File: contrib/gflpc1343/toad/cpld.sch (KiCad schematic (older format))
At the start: 30 parts, among them P1 GOODFET, P2 CPLD_JTAG, P4 EXPANSION, U27 DG409, U28 5M80ZT100, U29 GSG-AD5290, U30 DG409, U31 MC4558

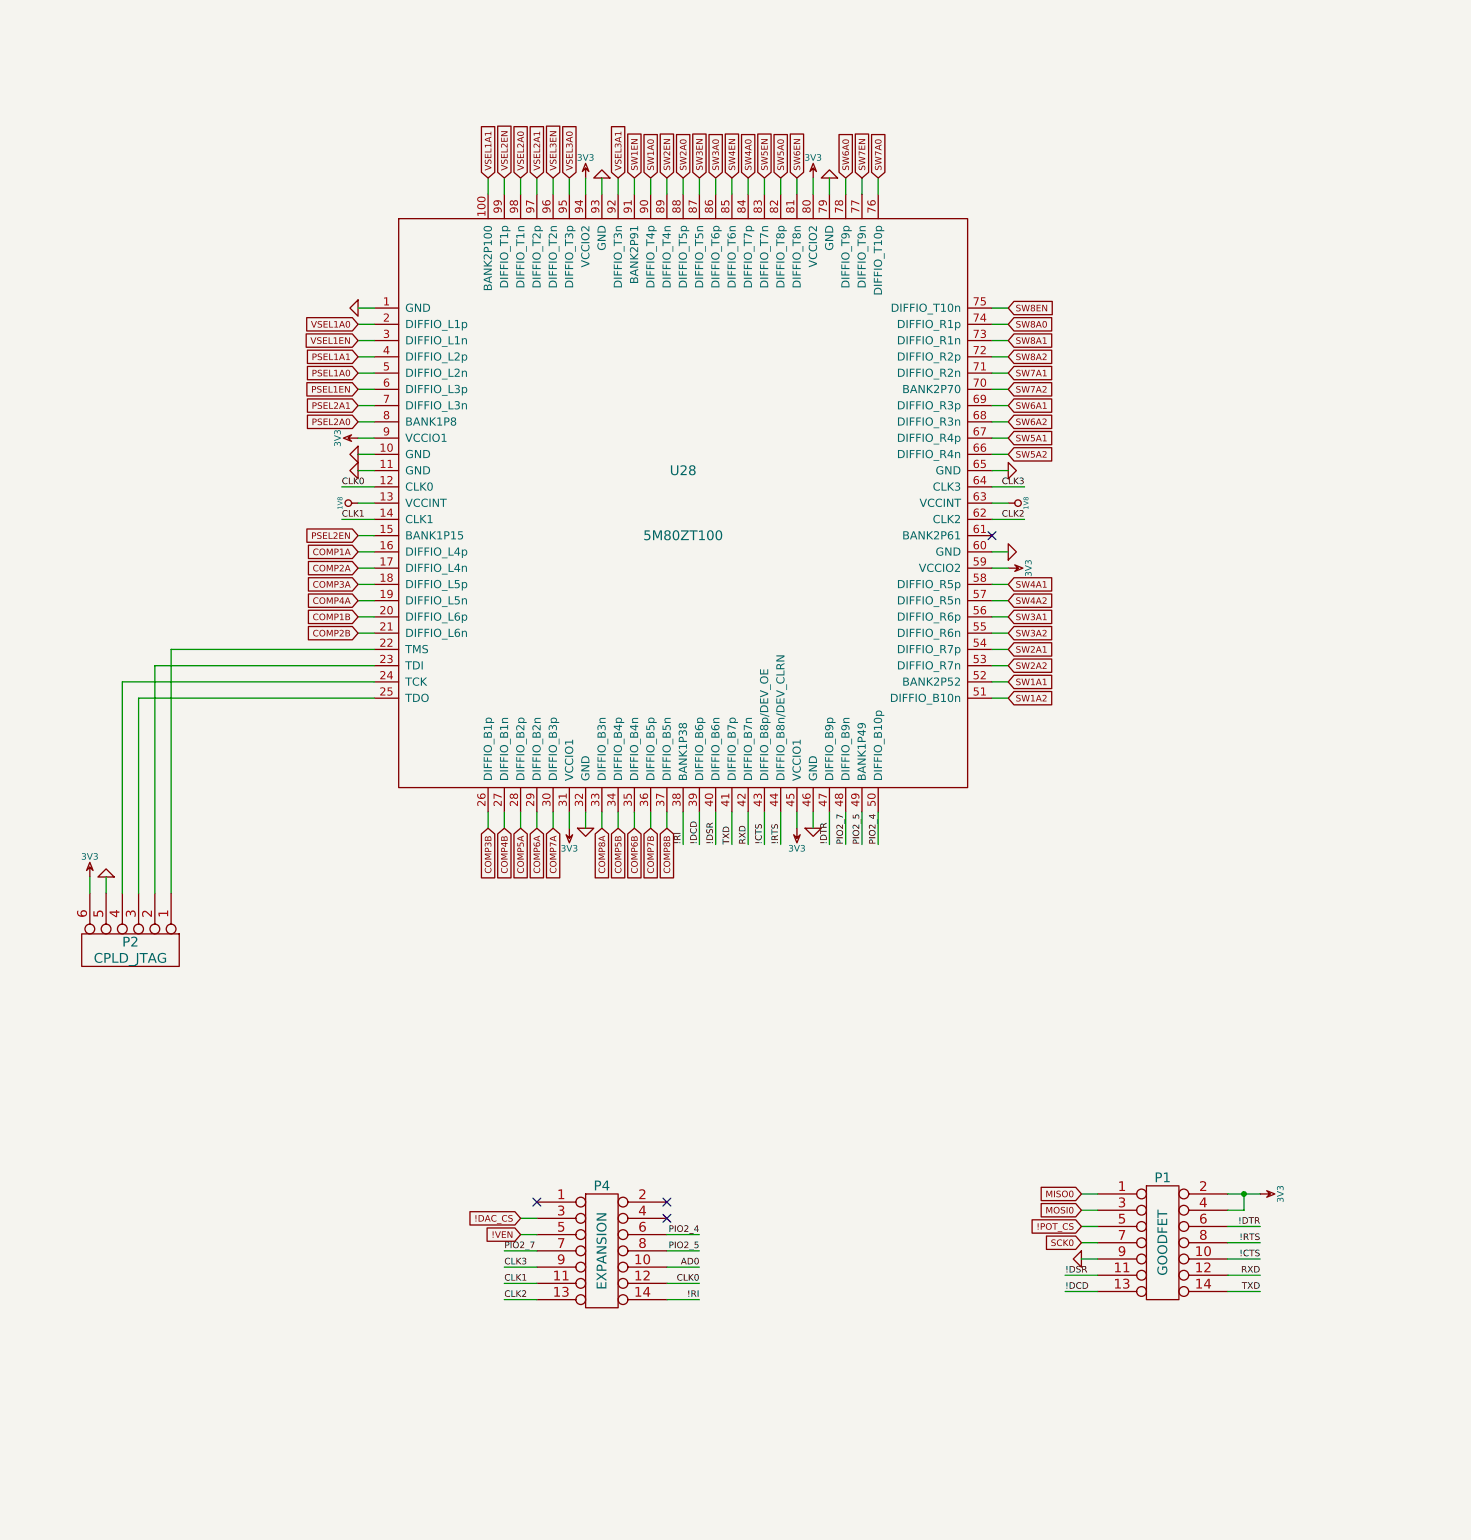
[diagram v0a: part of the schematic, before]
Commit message: TOAD: CPLD decoupling caps, rearranged headers to expose JTAG, etc.
git-svn-id: https://svn.code.sf.net/p/goodfet/code@1622 12e2690d-a6be-4b82-a7b7-67c4a43b65c8
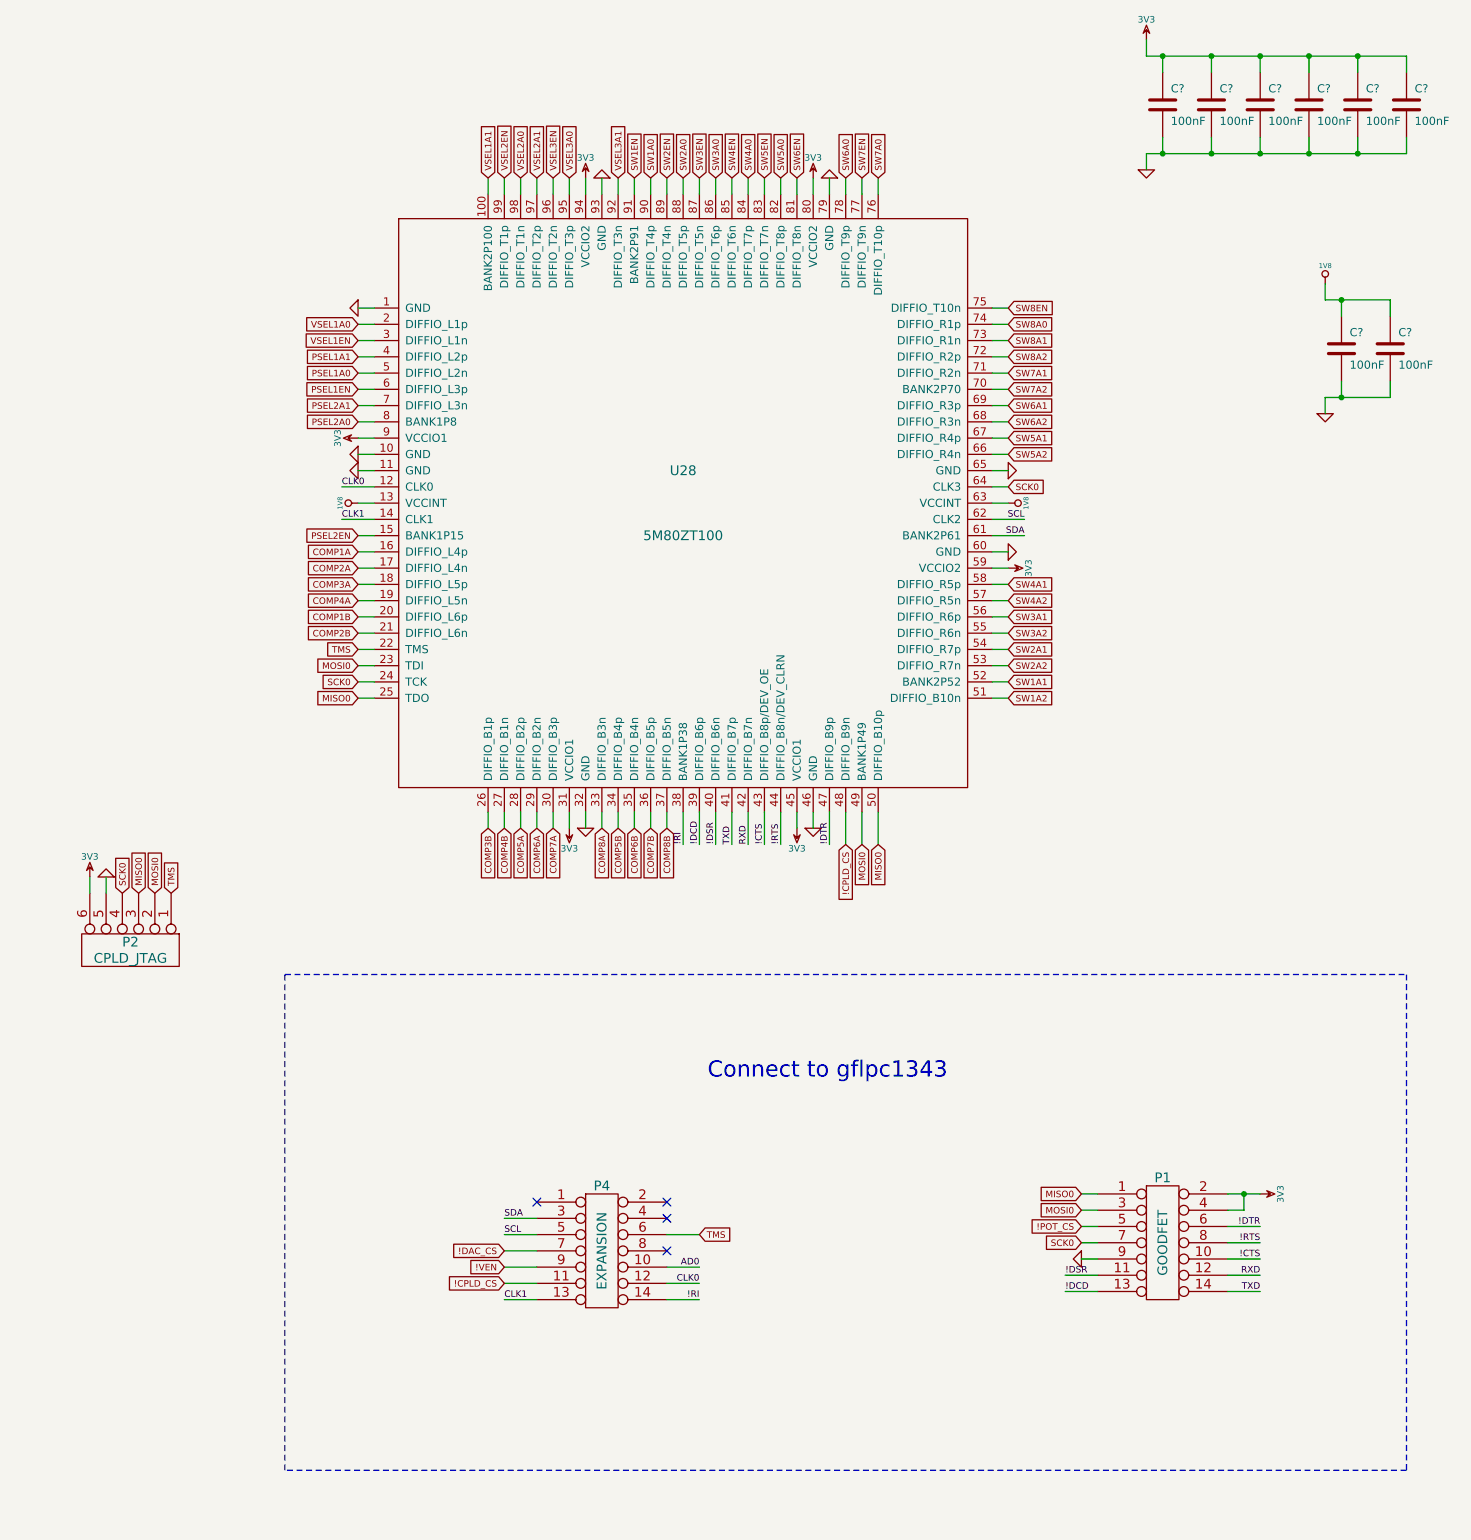
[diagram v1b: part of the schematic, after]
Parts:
- added C? (x8): 100nF, symbol C
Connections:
- net !DAC_CS: now also P4.7 (P7); no longer P4.3 (P3)
- net !VEN: now also P4.9; no longer P4.5 (P5)
- net +1.8V: now also C?.1, C?.1
- net 3V3: now also C?.1, C?.1, C?.1, C?.1, C?.1, C?.1
- net CLK1: now also P4.13; no longer P4.11
- net GND: now also C?.2, C?.2, C?.2, C?.2, C?.2, C?.2, C?.2, C?.2
- net MISO0: now also P2.3, U28.25 (TDO), U28.50 (DIFFIO_B10p)
- net MOSI0: now also P2.2, U28.23 (TDI), U28.49 (BANK1P49)
- net SCK0: now also P2.4, U28.24 (TCK), U28.64 (CLK3)
- net TMS: now reaches P2.1, U28.22 (TMS)
- net TMS: now also P4.6 (P6)
- net SDA: now reaches U28.61 (BANK2P61)
- net SDA: now also P4.3 (P3)
- net CLK2 renamed SCL
- net SCL: now also P4.5 (P5); no longer P4.13
- removed net CLK3: P4.9, U28.64 (CLK3)
- removed net PIO2_4: P4.6 (P6), U28.50 (DIFFIO_B10p)
- net PIO2_5: no longer names the net of P4.8 (P8)
- net PIO2_5: no longer U28.49 (BANK1P49)
- net PIO2_7 renamed !CPLD_CS
- net !CPLD_CS: now also P4.11; no longer P4.7 (P7)
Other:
- note added: "Connect to gflpc1343"

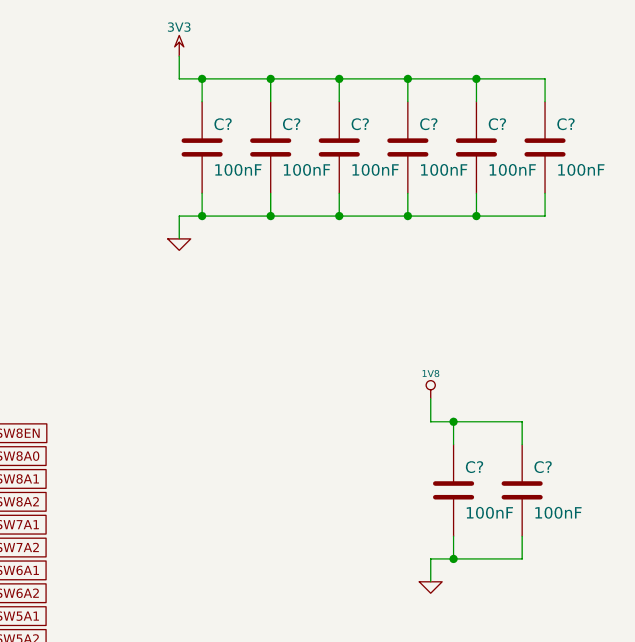
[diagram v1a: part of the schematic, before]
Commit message: TOAD: power indicator LED, some component selection
git-svn-id: https://svn.code.sf.net/p/goodfet/code@1623 12e2690d-a6be-4b82-a7b7-67c4a43b65c8
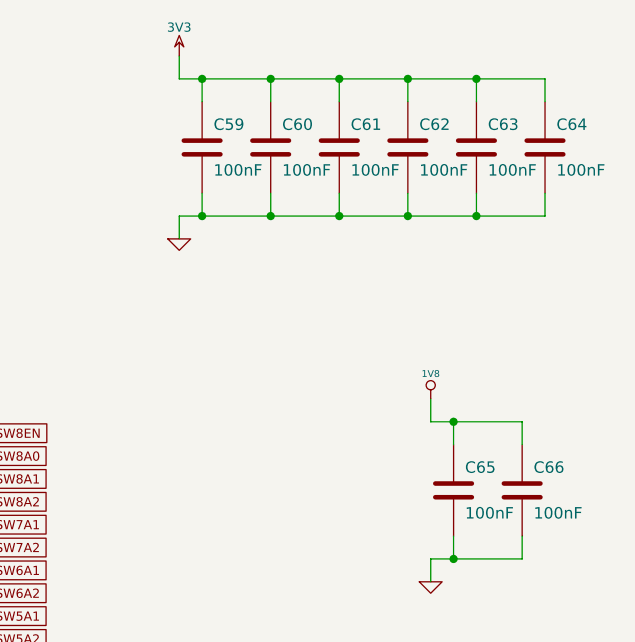
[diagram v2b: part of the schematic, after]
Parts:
- U27, U30: Description (none) -> IC MUX CMOS ANG DUAL 8CH 16TSSOP; Manufacturer (none) -> Vishay Siliconix; Part Number (none) -> DG409LDQ-T1-E3
- U28: Description (none) -> IC MAX V CPLD 80 LE 100-TQFP; Manufacturer (none) -> Altera; Part Number (none) -> 5M80ZT100C5N
- gave numbers to parts that had none: 8

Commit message: TOAD: comparator voltage dividers
git-svn-id: https://svn.code.sf.net/p/goodfet/code@1624 12e2690d-a6be-4b82-a7b7-67c4a43b65c8
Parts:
- added R100, R101, R102, R107, R108, R109, R110, R115, R116, R117, R118, R91, R92, R93, R99: 49.9k, symbol R
- added R103, R104, R105, R106, R111, R112, R113, R114, R119, R120, R121, R122, R95, R96, R97, R98: 249k, symbol R
- added R94: 49.9, symbol R
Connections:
- net 3V3: now also R100.1, R101.1, R102.1, R107.1, R108.1, R109.1, R110.1, R115.1, R116.1, R117.1, R118.1, R91.1, R92.1, R93.1, R94.1, R99.1
- net COMP1A: now also R95.1; no longer U28.16 (DIFFIO_L4p)
- net COMP1B: now also R103.1; no longer U28.20 (DIFFIO_L6p)
- net COMP2A: now also R96.1; no longer U28.17 (DIFFIO_L4n)
- net COMP2B: now also R104.1; no longer U28.21 (DIFFIO_L6n)
- net COMP3A: now also R97.1; no longer U28.18 (DIFFIO_L5p)
- net COMP3B: now also R105.1; no longer U28.26 (DIFFIO_B1p)
- net COMP4A: now also R98.1; no longer U28.19 (DIFFIO_L5n)
- net COMP4B: now also R106.1; no longer U28.27 (DIFFIO_B1n)
- net COMP5A: now also R111.1; no longer U28.28 (DIFFIO_B2p)
- net COMP5B: now also R119.1; no longer U28.34 (DIFFIO_B4p)
- net COMP6A: now also R112.1; no longer U28.29 (DIFFIO_B2n)
- net COMP6B: now also R120.1; no longer U28.35 (DIFFIO_B4n)
- net COMP7A: now also R113.1; no longer U28.30 (DIFFIO_B3p)
- net COMP7B: now also R121.1; no longer U28.36 (DIFFIO_B5p)
- net COMP8A: now also R114.1; no longer U28.33 (DIFFIO_B3n)
- net COMP8B: now also R122.1; no longer U28.37 (DIFFIO_B5n)
- net GND: now also U31.2 (I1-), U31.3 (I1+)
- new net: R94.2, R95.2, U28.16 (DIFFIO_L4p)
- new net: R93.2, R96.2, U28.17 (DIFFIO_L4n)
- new net: R92.2, R97.2, U28.18 (DIFFIO_L5p)
- new net: R91.2, R98.2, U28.19 (DIFFIO_L5n)
- new net: R102.2, R103.2, U28.20 (DIFFIO_L6p)
- new net: R101.2, R104.2, U28.21 (DIFFIO_L6n)
- new net: R100.2, R105.2, U28.26 (DIFFIO_B1p)
- new net: R106.2, R99.2, U28.27 (DIFFIO_B1n)
- new net: R110.2, R111.2, U28.28 (DIFFIO_B2p)
- new net: R109.2, R112.2, U28.29 (DIFFIO_B2n)
- new net: R108.2, R113.2, U28.30 (DIFFIO_B3p)
- new net: R107.2, R114.2, U28.33 (DIFFIO_B3n)
- new net: R118.2, R119.2, U28.34 (DIFFIO_B4p)
- new net: R117.2, R120.2, U28.35 (DIFFIO_B4n)
- new net: R116.2, R121.2, U28.36 (DIFFIO_B5p)
- new net: R115.2, R122.2, U28.37 (DIFFIO_B5n)
- no-connect marks 7 -> 5
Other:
- moved on the sheet: C56, C57, C58, P2, R84, R85, R86, R87, R88, R89, U28, U31

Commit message: completed TOAD design
git-svn-id: https://svn.code.sf.net/p/goodfet/code@1656 12e2690d-a6be-4b82-a7b7-67c4a43b65c8
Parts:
- added C67, C68: 100nF, symbol C
- R94: value 49.9 -> 49.9k
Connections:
- net !CPLD_CS: now also U28.8 (BANK1P8); no longer U28.48 (DIFFIO_B9n)
- net !CTS: now also U28.58 (DIFFIO_R5p); no longer U28.43 (DIFFIO_B8p/DEV_OE)
- net !DCD: now also U28.54 (DIFFIO_R7p); no longer U28.39 (DIFFIO_B6p)
- net !DSR: now also U28.56 (DIFFIO_R6p); no longer U28.40 (DIFFIO_B6n)
- net !DTR: now also U28.67 (DIFFIO_R4p); no longer U28.47 (DIFFIO_B9p)
- net !RI: now also U28.7 (DIFFIO_L3n); no longer U28.38 (BANK1P38)
- net !RTS: now also U28.66 (DIFFIO_R4n); no longer U28.44 (DIFFIO_B8n/DEV_CLRN)
- net 3V3: now also P4.2 (P2); no longer P1.2 (P2), P1.4 (P4)
- net GND: now also P4.1 (P1), C67.2, C68.2; no longer P1.9
- net MISO0: now also U28.69 (DIFFIO_R3p); no longer U28.50 (DIFFIO_B10p)
- net MOSI0: now also U28.68 (DIFFIO_R3n); no longer U28.49 (BANK1P49)
- net PSEL1A0: now also U28.33 (DIFFIO_B3n); no longer U28.5 (DIFFIO_L2n)
- net PSEL1A1: now also U28.35 (DIFFIO_B4n); no longer U28.4 (DIFFIO_L2p)
- net PSEL1EN: now also U28.34 (DIFFIO_B4p); no longer U28.6 (DIFFIO_L3p)
- net PSEL2A0: now also U28.17 (DIFFIO_L4n); no longer U28.8 (BANK1P8)
- net PSEL2A1: now also U28.15 (BANK1P15); no longer U28.7 (DIFFIO_L3n)
- net PSEL2EN: now also U28.16 (DIFFIO_L4p); no longer U28.15 (BANK1P15)
- net RXD: now also U28.57 (DIFFIO_R5n); no longer U28.42 (DIFFIO_B7n)
- net SW1A0: now also U28.42 (DIFFIO_B7n); no longer U28.90 (DIFFIO_T4p)
- net SW1A1: now also U28.97 (DIFFIO_T2p); no longer U28.52 (BANK2P52)
- net SW1A2: now also U28.96 (DIFFIO_T2n); no longer U28.51 (DIFFIO_B10n)
- net SW1EN: now also U28.43 (DIFFIO_B8p/DEV_OE); no longer U28.91 (BANK2P91)
- net SW2A0: now also U28.40 (DIFFIO_B6n); no longer U28.88 (DIFFIO_T5p)
- net SW2A1: now also U28.95 (DIFFIO_T3p); no longer U28.54 (DIFFIO_R7p)
- net SW2A2: now also U28.92 (DIFFIO_T3n); no longer U28.53 (DIFFIO_R7n)
- net SW2EN: now also U28.41 (DIFFIO_B7p); no longer U28.89 (DIFFIO_T4n)
- net SW3A0: now also U28.38 (BANK1P38); no longer U28.86 (DIFFIO_T6p)
- net SW3A1: now also U28.91 (BANK2P91); no longer U28.56 (DIFFIO_R6p)
- net SW3A2: now also U28.90 (DIFFIO_T4p); no longer U28.55 (DIFFIO_R6n)
- net SW3EN: now also U28.39 (DIFFIO_B6p); no longer U28.87 (DIFFIO_T5n)
- net SW4A0: now also U28.36 (DIFFIO_B5p); no longer U28.84 (DIFFIO_T7p)
- net SW4A1: now also U28.89 (DIFFIO_T4n); no longer U28.58 (DIFFIO_R5p)
- net SW4A2: now also U28.88 (DIFFIO_T5p); no longer U28.57 (DIFFIO_R5n)
- net SW4EN: now also U28.37 (DIFFIO_B5n); no longer U28.85 (DIFFIO_T6n)
- net SW5A0: now also U28.71 (DIFFIO_R2n); no longer U28.82 (DIFFIO_T8p)
- net SW5A1: now also U28.87 (DIFFIO_T5n); no longer U28.67 (DIFFIO_R4p)
- net SW5A2: now also U28.86 (DIFFIO_T6p); no longer U28.66 (DIFFIO_R4n)
- net SW5EN: now also U28.70 (BANK2P70); no longer U28.83 (DIFFIO_T7n)
- net SW6A0: now also U28.53 (DIFFIO_R7n); no longer U28.78 (DIFFIO_T9p)
- net SW6A1: now also U28.85 (DIFFIO_T6n); no longer U28.69 (DIFFIO_R3p)
- net SW6A2: now also U28.84 (DIFFIO_T7p); no longer U28.68 (DIFFIO_R3n)
- net SW6EN: now also U28.52 (BANK2P52); no longer U28.81 (DIFFIO_T8n)
- net SW7A0: now also U28.49 (BANK1P49); no longer U28.76 (DIFFIO_T10p)
- net SW7A1: now also U28.83 (DIFFIO_T7n); no longer U28.71 (DIFFIO_R2n)
- net SW7A2: now also U28.82 (DIFFIO_T8p); no longer U28.70 (BANK2P70)
- net SW7EN: now also U28.48 (DIFFIO_B9n); no longer U28.77 (DIFFIO_T9n)
- net SW8A0: now also U28.47 (DIFFIO_B9p); no longer U28.74 (DIFFIO_R1p)
- net SW8A1: now also U28.81 (DIFFIO_T8n); no longer U28.73 (DIFFIO_R1n)
- net SW8A2: now also U28.78 (DIFFIO_T9p); no longer U28.72 (DIFFIO_R2p)
- net SW8EN: now also U28.44 (DIFFIO_B8n/DEV_CLRN); no longer U28.75 (DIFFIO_T10n)
- net TXD: now also U28.55 (DIFFIO_R6n); no longer U28.41 (DIFFIO_B7p)
- net V+: now also C67.1
- net V-: now also C68.1
- net VSEL1A0: now also U28.27 (DIFFIO_B1n); no longer U28.2 (DIFFIO_L1p)
- net VSEL1A1: now also U28.26 (DIFFIO_B1p); no longer U28.100 (BANK2P100)
- net VSEL1EN: now also U28.21 (DIFFIO_L6n); no longer U28.3 (DIFFIO_L1n)
- net VSEL2A0: now also U28.30 (DIFFIO_B3p); no longer U28.98 (DIFFIO_T1n)
- net VSEL2A1: now also U28.29 (DIFFIO_B2n); no longer U28.97 (DIFFIO_T2p)
- net VSEL2EN: now also U28.28 (DIFFIO_B2p); no longer U28.99 (DIFFIO_T1p)
- net VSEL3A0: now also U28.18 (DIFFIO_L5p); no longer U28.95 (DIFFIO_T3p)
- net VSEL3A1: now also U28.20 (DIFFIO_L6p); no longer U28.92 (DIFFIO_T3n)
- net VSEL3EN: now also U28.19 (DIFFIO_L5n); no longer U28.96 (DIFFIO_T2n)
- net at R94.2, R95.2: now also U28.3 (DIFFIO_L1n); no longer U28.16 (DIFFIO_L4p)
- net at R93.2, R96.2: now also U28.4 (DIFFIO_L2p); no longer U28.17 (DIFFIO_L4n)
- net at R92.2, R97.2: now also U28.5 (DIFFIO_L2n); no longer U28.18 (DIFFIO_L5p)
- net at R91.2, R98.2: now also U28.6 (DIFFIO_L3p); no longer U28.19 (DIFFIO_L5n)
- net at R102.2, R103.2: now also U28.98 (DIFFIO_T1n); no longer U28.20 (DIFFIO_L6p)
- net at R101.2, R104.2: now also U28.99 (DIFFIO_T1p); no longer U28.21 (DIFFIO_L6n)
- net at R100.2, R105.2: now also U28.100 (BANK2P100); no longer U28.26 (DIFFIO_B1p)
- net at R106.2, R99.2: now also U28.2 (DIFFIO_L1p); no longer U28.27 (DIFFIO_B1n)
- net at R110.2, R111.2: now also U28.73 (DIFFIO_R1n); no longer U28.28 (DIFFIO_B2p)
- net at R109.2, R112.2: now also U28.72 (DIFFIO_R2p); no longer U28.29 (DIFFIO_B2n)
- net at R108.2, R113.2: now also U28.50 (DIFFIO_B10p); no longer U28.30 (DIFFIO_B3p)
- net at R107.2, R114.2: now also U28.51 (DIFFIO_B10n); no longer U28.33 (DIFFIO_B3n)
- net at R118.2, R119.2: now also U28.75 (DIFFIO_T10n); no longer U28.34 (DIFFIO_B4p)
- net at R117.2, R120.2: now also U28.74 (DIFFIO_R1p); no longer U28.35 (DIFFIO_B4n)
- net at R116.2, R121.2: now also U28.76 (DIFFIO_T10p); no longer U28.36 (DIFFIO_B5p)
- net at R115.2, R122.2: now also U28.77 (DIFFIO_T9n); no longer U28.37 (DIFFIO_B5n)
- no-connect marks 5 -> 6
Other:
- moved on the sheet: R100, R101, R102, R103, R104, R105, R106, R115, R116, R117, R118, R119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

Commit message: TOAD: fixed part numbers for DG408/DG409
git-svn-id: https://svn.code.sf.net/p/goodfet/code@1660 12e2690d-a6be-4b82-a7b7-67c4a43b65c8
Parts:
- U27, U30: Part Number DG409LDQ-T1-E3 -> DG409DQ-T1-E3
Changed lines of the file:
@@
 F 1 "DG409" V 1800 2250 60  0000 C CNN
 F 4 "Vishay Siliconix" H 1850 2250 60  0001 C CNN "Manufacturer"
-F 5 "DG409LDQ-T1-E3" H 1850 2250 60  0001 C CNN "Part Number"
+F 5 "DG409DQ-T1-E3" H 1850 2250 60  0001 C CNN "Part Number"
 F 6 "IC MUX CMOS ANG DUAL 8CH 16TSSOP" H 1850 2250 60  0001 C CNN "Description"
 	1    1850 2250
@@
 F 1 "DG409" V 1800 6750 60  0000 C CNN
 F 4 "Vishay Siliconix" H 1850 6750 60  0001 C CNN "Manufacturer"
-F 5 "DG409LDQ-T1-E3" H 1850 6750 60  0001 C CNN "Part Number"
+F 5 "DG409DQ-T1-E3" H 1850 6750 60  0001 C CNN "Part Number"
 F 6 "IC MUX CMOS ANG DUAL 8CH 16TSSOP" H 1850 6750 60  0001 C CNN "Description"
 	1    1850 6750
